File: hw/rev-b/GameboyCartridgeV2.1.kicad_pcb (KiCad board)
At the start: 4 copper layers, 52.8 x 61.2 mm, 81 parts, among them J1 USB_C_Receptacle_USB2.0, J2 Micro_SD_Card_Det2, J3 DBG_UART, J4 Conn_01x06, J5 CartBus, Q1 CJ2302, SW1 SW_Push, SW2 SW_Push, U1 USBLC6-2P6, U2 W25Q16JVSSIQ, U3 RP2350_80QFN, U4 W956A8MBYA5I, U5 MCP79510, U6 AP2112K-3.3, U7 TXB0108PW, Y1 12MHz, Y2 32.768kHz

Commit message: board: scripted schematic->PCB update (70 footprints staged, nets, rip of USB_D_prot pair), deterministic sheet UUIDs, U106 to SM8 for clearance; parity pass; logbook
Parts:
- added C101: 1uF 25V X5R, Capacitor_SMD:C_0402_1005Metric, F.Cu at (175.0, 60.0)
- added C102: 1uF 25V X5R, Capacitor_SMD:C_0402_1005Metric, F.Cu at (183.0, 60.0)
- added C103: 1uF 25V X5R, Capacitor_SMD:C_0402_1005Metric, F.Cu at (191.0, 60.0)
- added C104: 1uF 25V X5R, Capacitor_SMD:C_0402_1005Metric, F.Cu at (199.0, 60.0)
- added C105: 330uF 6.3V 25mOhm 6TPE330MAP, Capacitor_Tantalum_SMD:CP_EIA-7343-20_Kemet-V, F.Cu at (207.0, 60.0)
- added C106: 330uF 6.3V 25mOhm 6TPE330MAP, Capacitor_Tantalum_SMD:CP_EIA-7343-20_Kemet-V, F.Cu at (215.0, 60.0)
- added C107: 330uF 6.3V 25mOhm 6TPE330MAP, Capacitor_Tantalum_SMD:CP_EIA-7343-20_Kemet-V, F.Cu at (175.0, 68.0)
- added C108: 10uF 10V X5R, Capacitor_SMD:C_0603_1608Metric, F.Cu at (183.0, 68.0)
- added C109: 10uF 10V X5R, Capacitor_SMD:C_0603_1608Metric, F.Cu at (191.0, 68.0)
- added C110: 22uF 6.3V X5R, Capacitor_SMD:C_0603_1608Metric, F.Cu at (199.0, 68.0)
- added C111: 10uF 10V X5R, Capacitor_SMD:C_0603_1608Metric, F.Cu at (207.0, 68.0)
- added C112: 100nF 16V X7R, Capacitor_SMD:C_0402_1005Metric, F.Cu at (215.0, 68.0)
- added C113: 100nF 16V X7R, Capacitor_SMD:C_0402_1005Metric, F.Cu at (175.0, 76.0)
- added C114: 2.2nF 50V X7R, Capacitor_SMD:C_0402_1005Metric, F.Cu at (183.0, 76.0)
- added C115: 2.2nF 50V X7R, Capacitor_SMD:C_0402_1005Metric, F.Cu at (191.0, 76.0)
- added C116: 100nF 16V X7R, Capacitor_SMD:C_0402_1005Metric, F.Cu at (199.0, 76.0)
- added C117: 100nF 16V X7R, Capacitor_SMD:C_0402_1005Metric, F.Cu at (207.0, 76.0)
- added C118: 1uF 25V X5R, Capacitor_SMD:C_0402_1005Metric, F.Cu at (215.0, 76.0)
- added C119: 1uF 25V X5R, Capacitor_SMD:C_0402_1005Metric, F.Cu at (175.0, 84.0)
- added C120: 100nF 16V X7R, Capacitor_SMD:C_0402_1005Metric, F.Cu at (183.0, 84.0)
- added C121: 10nF 50V X7R, Capacitor_SMD:C_0402_1005Metric, F.Cu at (191.0, 84.0)
- added C122: 100nF 16V X7R, Capacitor_SMD:C_0402_1005Metric, F.Cu at (199.0, 84.0)
- added C123: 470pF 50V C0G, Capacitor_SMD:C_0402_1005Metric, F.Cu at (207.0, 84.0)
- added C124: 100nF 16V X7R, Capacitor_SMD:C_0402_1005Metric, F.Cu at (215.0, 84.0)
- added D101: 1N4148WS, Diode_SMD:D_SOD-323, F.Cu at (175.0, 92.0)
- added D102: 1N4148WS, Diode_SMD:D_SOD-323, F.Cu at (183.0, 92.0)
- added D103: 1N4148WS, Diode_SMD:D_SOD-323, F.Cu at (191.0, 92.0)
- added D104: 1N4148WS, Diode_SMD:D_SOD-323, F.Cu at (199.0, 92.0)
- added L101: 0.47uH 5.5A 26mOhm DFE201612E-R47M, Inductor_SMD:L_Murata_DFE201610P, F.Cu at (207.0, 92.0)
- added Q101: SIA975DJ-T1-GE3, Package_TO_SOT_SMD:Vishay_PowerPAK_SC70-6L_Dual, F.Cu at (215.0, 92.0)
- added Q102: 2N7002, Package_TO_SOT_SMD:SOT-23, F.Cu at (175.0, 100.0)
- added R101: 5.1k 1%, Resistor_SMD:R_0402_1005Metric, F.Cu at (183.0, 100.0)
- added R102: 2.0k 1%, Resistor_SMD:R_0402_1005Metric, F.Cu at (191.0, 100.0)
- added R103: 180k 1%, Resistor_SMD:R_0402_1005Metric, F.Cu at (199.0, 100.0)
- added R104: 100k 1%, Resistor_SMD:R_0402_1005Metric, F.Cu at (207.0, 100.0)
- added R108: 10k 1%, Resistor_SMD:R_0402_1005Metric, F.Cu at (215.0, 100.0)
- added R109: 511k 1%, Resistor_SMD:R_0402_1005Metric, F.Cu at (175.0, 108.0)
- added R110: 91k 1%, Resistor_SMD:R_0402_1005Metric, F.Cu at (183.0, 108.0)
- added R111: 10k 1%, Resistor_SMD:R_0402_1005Metric, F.Cu at (191.0, 108.0)
- added R112: 10k 1%, Resistor_SMD:R_0402_1005Metric, F.Cu at (199.0, 108.0)
- added R113: 10k 1%, Resistor_SMD:R_0402_1005Metric, F.Cu at (207.0, 108.0)
- added R114: 10k 1%, Resistor_SMD:R_0402_1005Metric, F.Cu at (215.0, 108.0)
- added R115: 100k 1%, Resistor_SMD:R_0402_1005Metric, F.Cu at (175.0, 116.0)
- added R116: 680k 1%, Resistor_SMD:R_0402_1005Metric, F.Cu at (183.0, 116.0)
- added R117: 200k 1%, Resistor_SMD:R_0402_1005Metric, F.Cu at (191.0, 116.0)
- added R118: 680k 1%, Resistor_SMD:R_0402_1005Metric, F.Cu at (199.0, 116.0)
- added R119: 200k 1%, Resistor_SMD:R_0402_1005Metric, F.Cu at (207.0, 116.0)
- added R120: 22R 1%, Resistor_SMD:R_0402_1005Metric, F.Cu at (215.0, 116.0)
- added R121: 22R 1%, Resistor_SMD:R_0402_1005Metric, F.Cu at (175.0, 124.0)
- added R122: 33R 1%, Resistor_SMD:R_0402_1005Metric, F.Cu at (183.0, 124.0)
- added R123: 1.3M 1%, Resistor_SMD:R_0402_1005Metric, F.Cu at (191.0, 124.0)
- added R124: 1.0M 1%, Resistor_SMD:R_0402_1005Metric, F.Cu at (199.0, 124.0)
- added R125: 1.2M 1%, Resistor_SMD:R_0402_1005Metric, F.Cu at (207.0, 124.0)
- added R126: 27.0k 0.1%, Resistor_SMD:R_0402_1005Metric, F.Cu at (215.0, 124.0)
- added R127: 10.0k 0.1%, Resistor_SMD:R_0402_1005Metric, F.Cu at (175.0, 132.0)
- added R128: 680 1%, Resistor_SMD:R_0402_1005Metric, F.Cu at (183.0, 132.0)
- added R129: 680 1%, Resistor_SMD:R_0402_1005Metric, F.Cu at (191.0, 132.0)
- added R130: 330k 1%, Resistor_SMD:R_0402_1005Metric, F.Cu at (199.0, 132.0)
- added R131: 470k 1%, Resistor_SMD:R_0402_1005Metric, F.Cu at (207.0, 132.0)
- added R132: 1k 1%, Resistor_SMD:R_0402_1005Metric, F.Cu at (215.0, 132.0)
- added U101: TPS2116DRLR, Package_TO_SOT_SMD:SOT-583-8, F.Cu at (175.0, 140.0)
- added U102: TPS2553DBVR, Package_TO_SOT_SMD:SOT-23-6, F.Cu at (183.0, 140.0)
- added U103: TPS63802DLAR, radio:TI_DLA0010A_VSON-HR-10_2x3mm_P0.5mm, F.Cu at (191.0, 140.0)
- added U104: ESP32-C3-MINI-1U-N4, radio:ESP32-C3-MINI-1U, F.Cu at (199.0, 140.0)
- added U105: SN74LVC1G125DBVR, Package_TO_SOT_SMD:SOT-23-5, F.Cu at (207.0, 140.0)
- added U106: SN74LVC3G34DCTR, Package_SO:SSOP-8_2.95x2.8mm_P0.65mm, F.Cu at (215.0, 140.0)
- added U107: CH334P, Package_DFN_QFN:QFN-16-1EP_3x3mm_P0.5mm_EP1.75x1.75mm, F.Cu at (175.0, 148.0)
- added U108: TLV3012BIDBVR, Package_TO_SOT_SMD:SOT-23-6, F.Cu at (183.0, 148.0)
- added U109: TLV431BIDBZR, Package_TO_SOT_SMD:SOT-23, F.Cu at (191.0, 148.0)
- added Y101: 12MHz 10pF 10ppm, Crystal:Crystal_SMD_3225-4Pin_3.2x2.5mm, F.Cu at (199.0, 148.0)
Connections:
- R10 pad 2: USB_D_prot- -> USB_RP_D-
- R9 pad 2: USB_D_prot+ -> USB_RP_D+
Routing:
- net USB_D_prot+: track 16.0 -> 0.00 mm, vias 2 -> 0
- net USB_D_prot-: track 16.0 -> 0.00 mm, vias 2 -> 0

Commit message: coin cell removed (DNP), RTC VBAT to GND per datasheet, power-symbol + dnp support in croco edit tool, board updated (BT1 off, +BATT ripped); logbook with save/RTC findings + correction
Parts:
- removed BT1: Battery_Cell, Battery:BatteryHolder_Keystone_3000_1x12mm
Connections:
- U5 pad 3: +BATT -> GND
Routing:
- net +BATT: track 7.88 -> 0.00 mm, vias 8 -> 0
- removed copper zone on In2.Cu, net +BATT

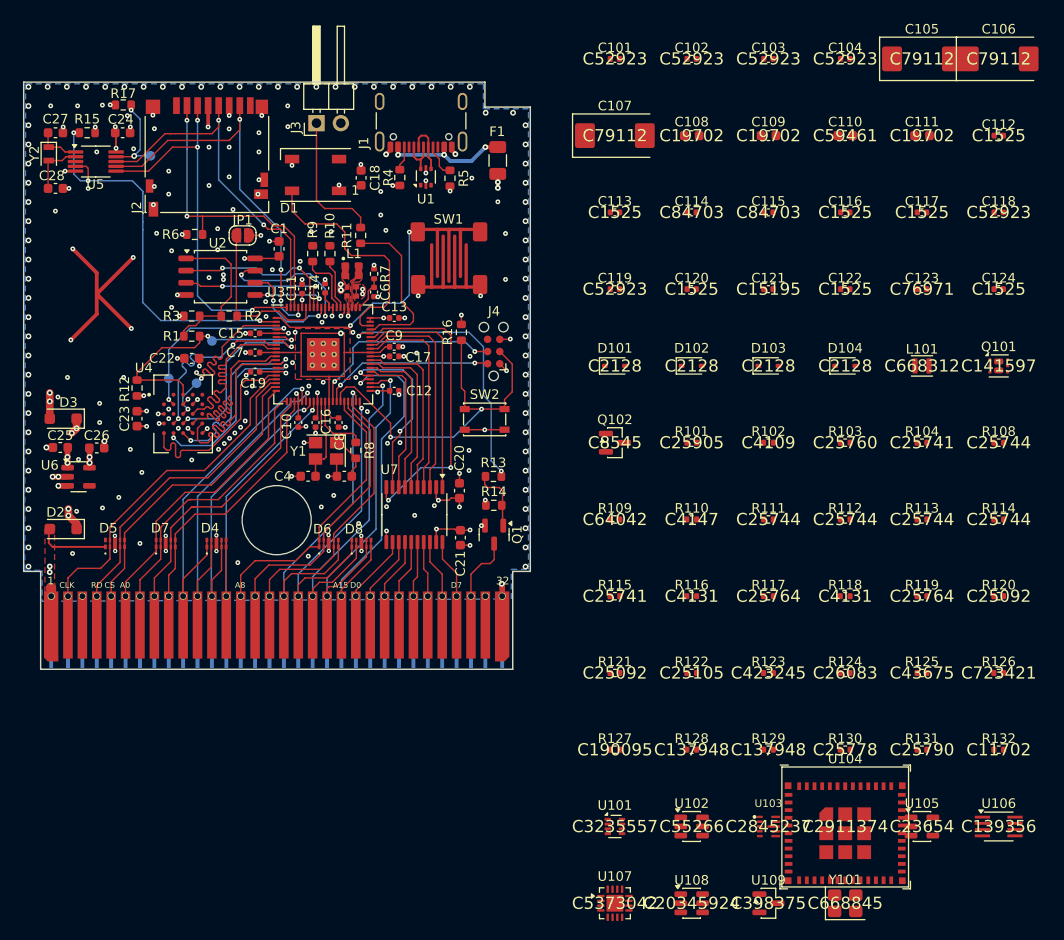
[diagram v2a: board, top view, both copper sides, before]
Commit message: layout: placement tooling (fit_part, place.py + placement.json), WiFi module placed in the former coin-cell area, BT1 GND stitching removed
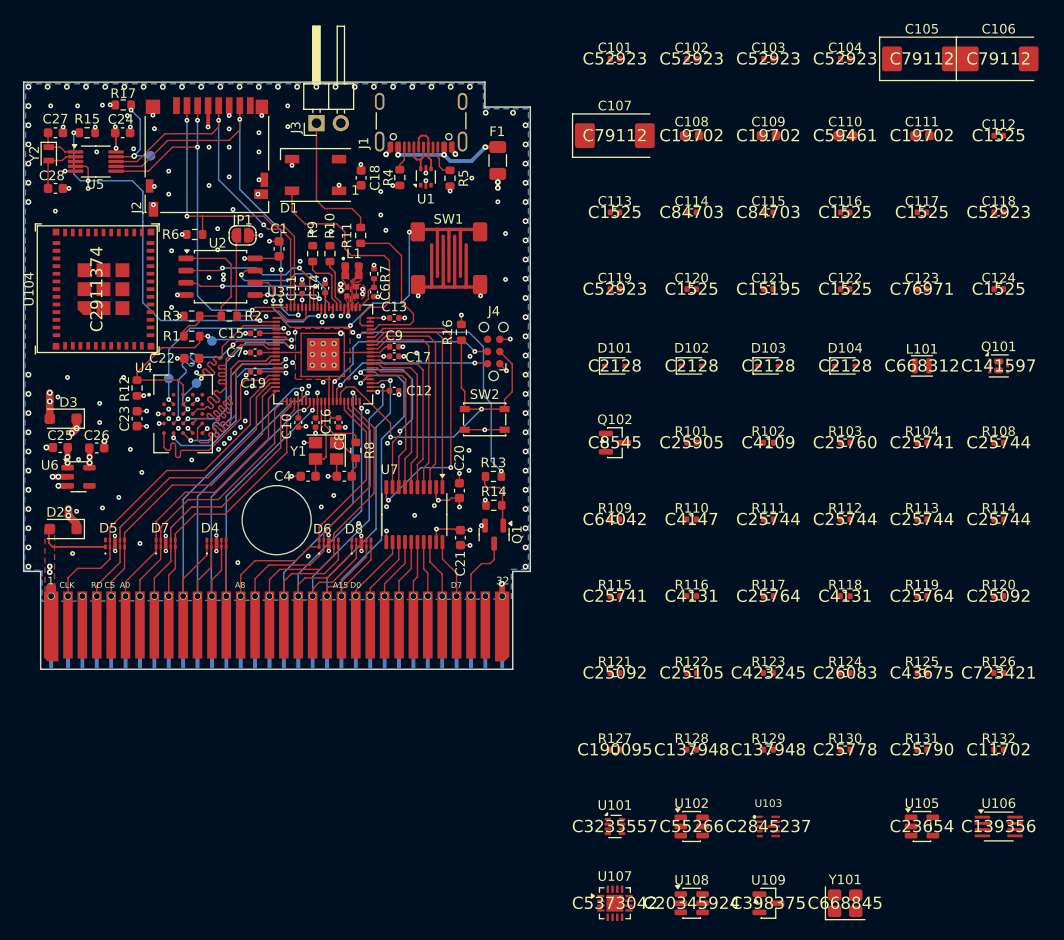
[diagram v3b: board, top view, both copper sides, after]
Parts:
- moved U104 96.0 mm to (121.0, 84.0), turned to 90 degrees
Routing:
- net GND: track 74.7 -> 52.6 mm, vias 234 -> 221

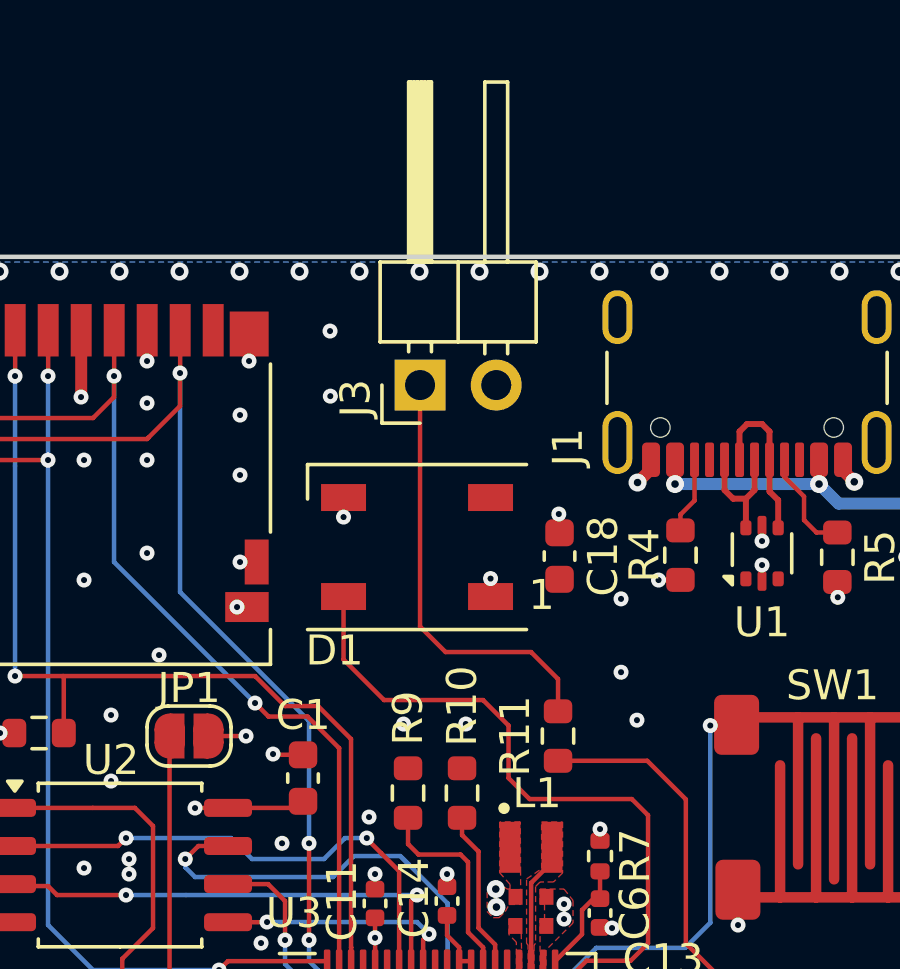
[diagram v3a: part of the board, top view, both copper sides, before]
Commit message: J3/R11 debug UART header DNP + off board (ESP CS stub), free-space map counts placed new parts, sim: firmware-configured vs actual reservoir C, T520B reservoir runs
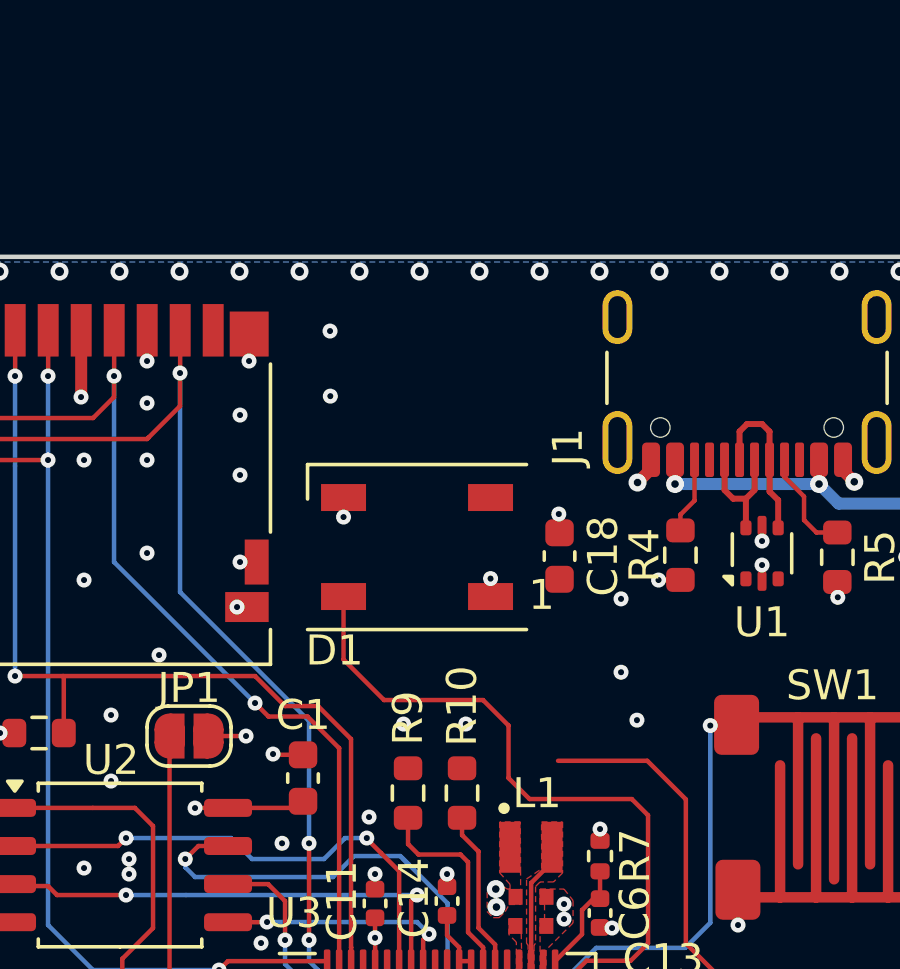
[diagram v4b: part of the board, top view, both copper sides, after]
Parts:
- removed J3: DBG_UART, Connector_PinHeader_2.54mm:PinHeader_1x02_P2.54mm_Horizontal
- removed R11: 10R, Resistor_SMD:R_0603_1608Metric
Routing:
- net Net-(J3-Pin_1): track 14.4 -> 0.00 mm

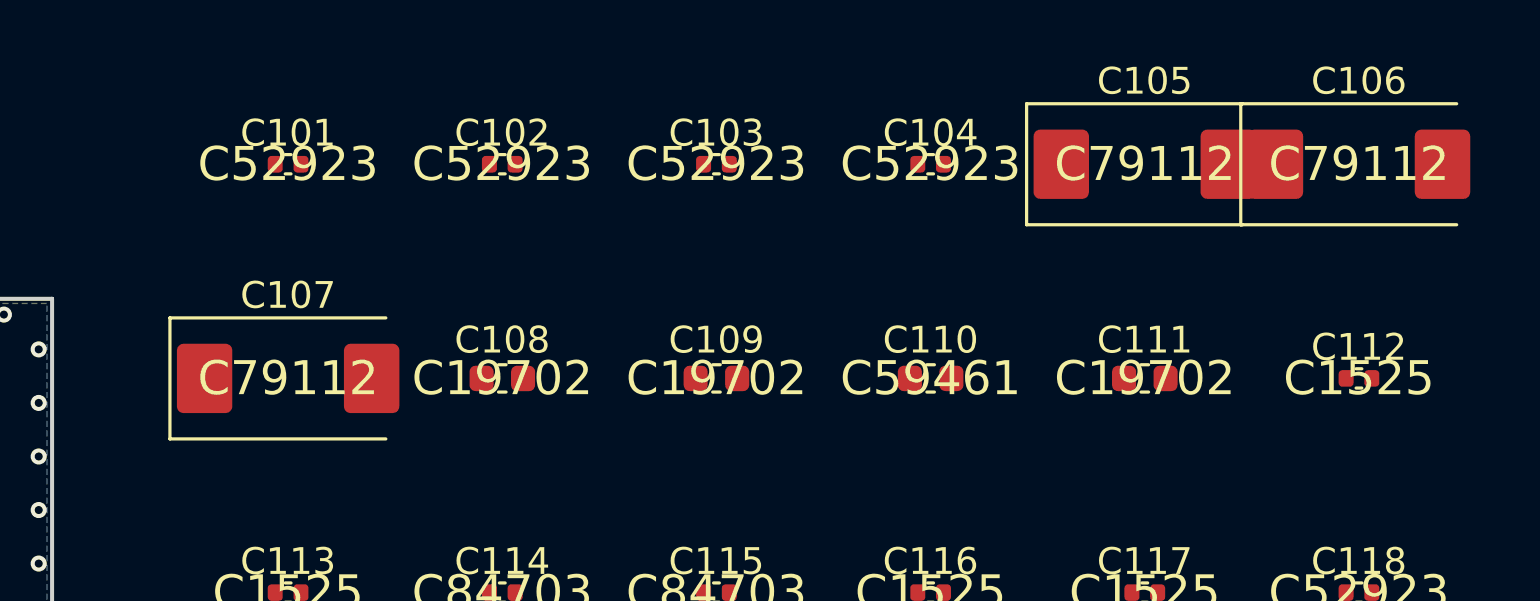
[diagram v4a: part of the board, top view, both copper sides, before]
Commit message: T520B reservoir (audits A1-A8 pass at -20% C), sim: firmware vs actual reservoir C, footprint swap in update_pcb, autoplace tool (result rejected, reverted), logbook
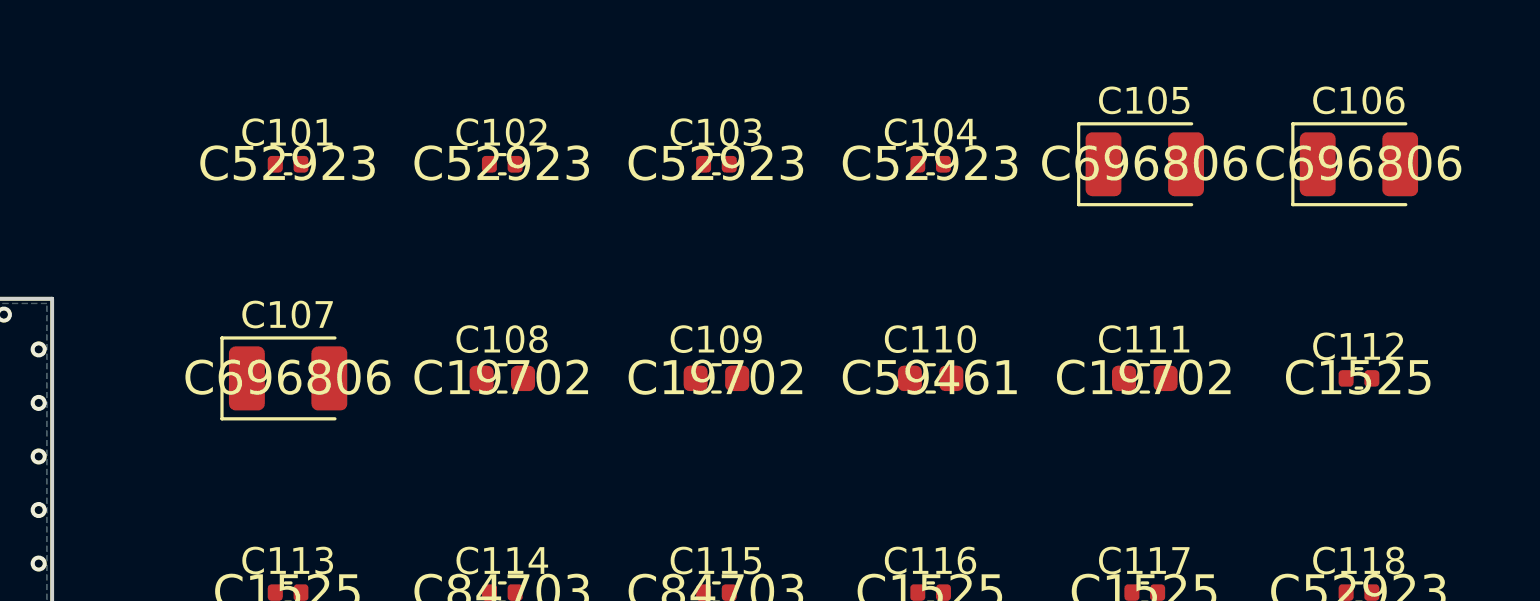
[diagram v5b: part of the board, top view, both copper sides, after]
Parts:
- C105, C106, C107: value 330uF 6.3V 25mOhm 6TPE330MAP -> 330uF 6.3V 40mOhm T520B337M006ATE040; footprint Capacitor_Tantalum_SMD:CP_EIA-7343-20_Kemet-V -> Capacitor_Tantalum_SMD:CP_EIA-3528-21_Kemet-B
